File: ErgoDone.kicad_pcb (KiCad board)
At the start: 2 copper layers, 173.3 x 158.9 mm, 149 parts, among them J1 USB, J2 3.5mm, J3 JMP, J4 JMP, SW0:10 SW0:3, SW0:11 SW0:2, SW0:12 SW0:1, SW0:7 SW0:6, SW0:8 SW0:5, SW0:9 SW0:4, SW1:10 SW1:3, SW1:11 SW1:2, SW1:12 SW1:1, SW1:13 SW1:0, SW1:9 SW1:4, SW2:10 SW2:3, SW2:11 SW2:2, SW2:12 SW2:1, SW2:13 SW2:0, SW2:7 SW2:6, SW2:8 SW2:5, SW2:9 SW2:4, SW3:10 SW3:3, SW3:11 SW3:2, SW3:12 SW3:1, SW3:13 SW3:0, SW3:7 SW3:6, SW3:8 SW3:5, SW3:9 SW3:4, SW4:10 SW4:3, SW4:11 SW4:2, SW4:12 SW4:1, SW4:13 SW4:0, SW4:7 SW4:6, SW4:8 SW4:5, SW4:9 SW4:4, SW5:10 SW5:3, SW5:11 SW5:2, SW5:12 SW5:1, SW5:13 SW5:0, SW5:7 SW5:6, SW5:8 SW5:5, SW5:9 SW5:4, U1 ProMicro, U2 MCP23017

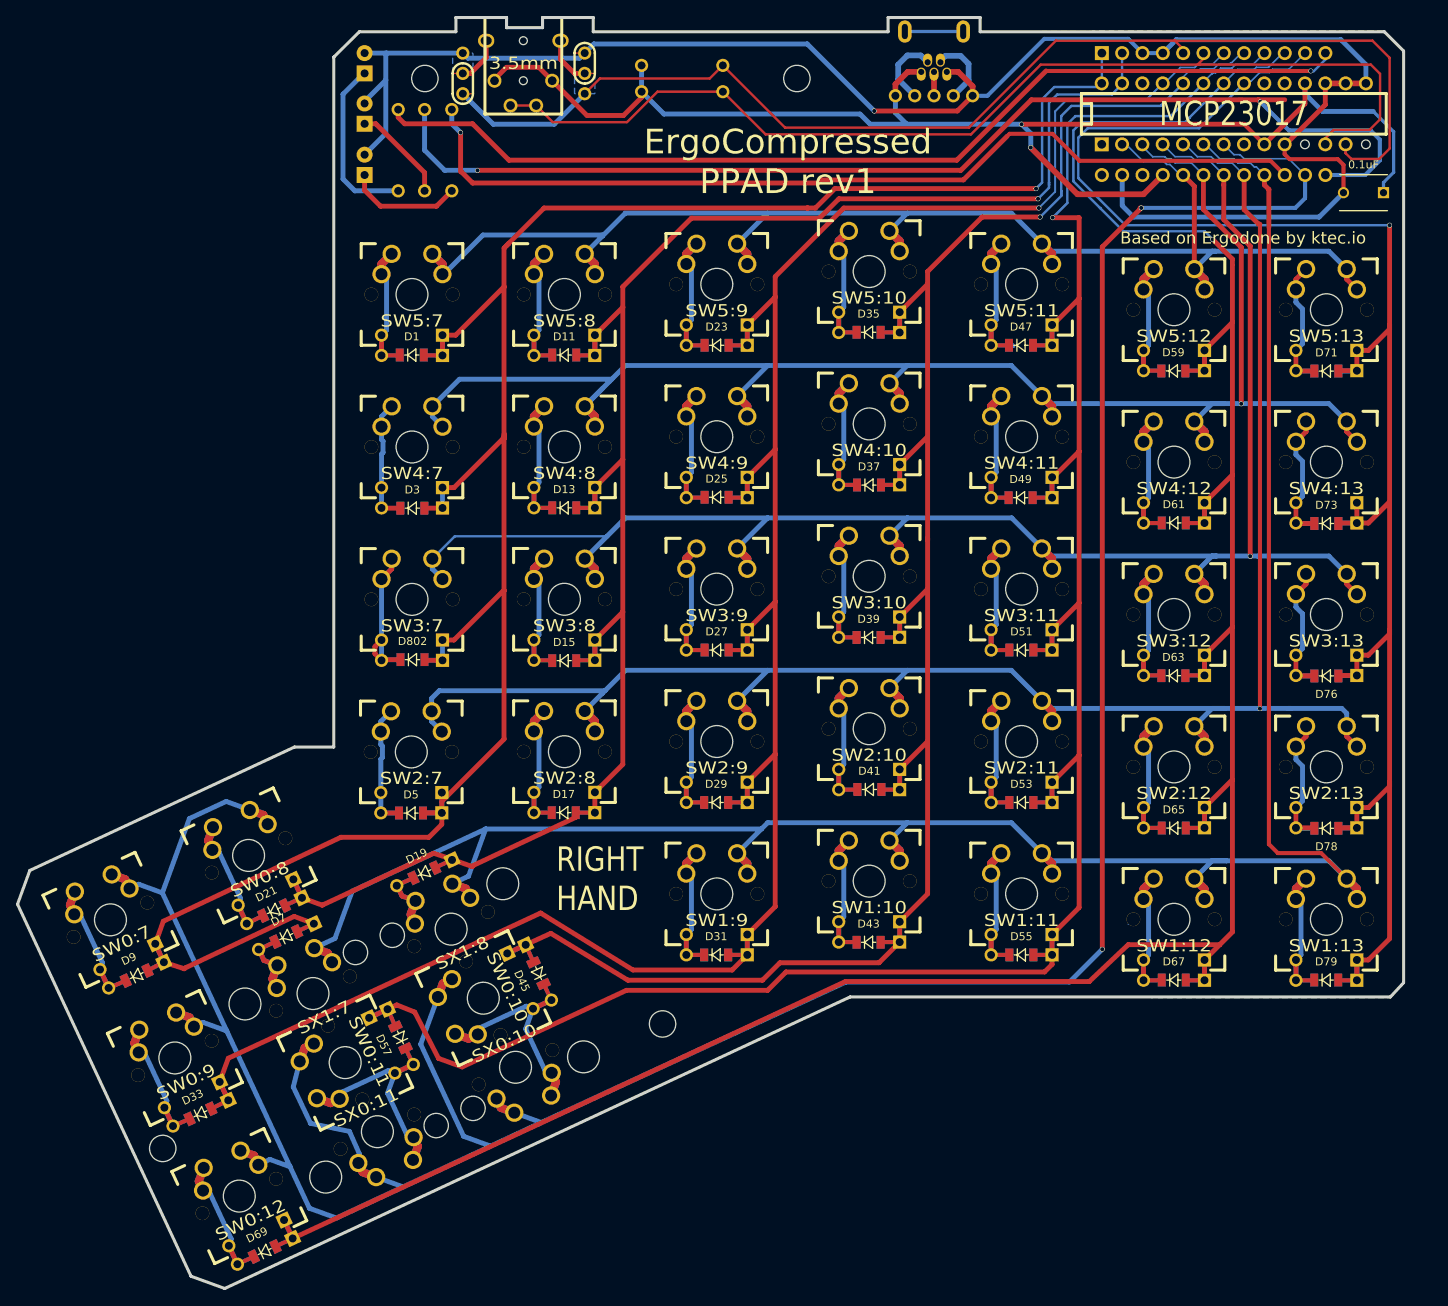
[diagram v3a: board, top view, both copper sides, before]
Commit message: Routing traces so the inner column of the thumb cluster could be safely removed.
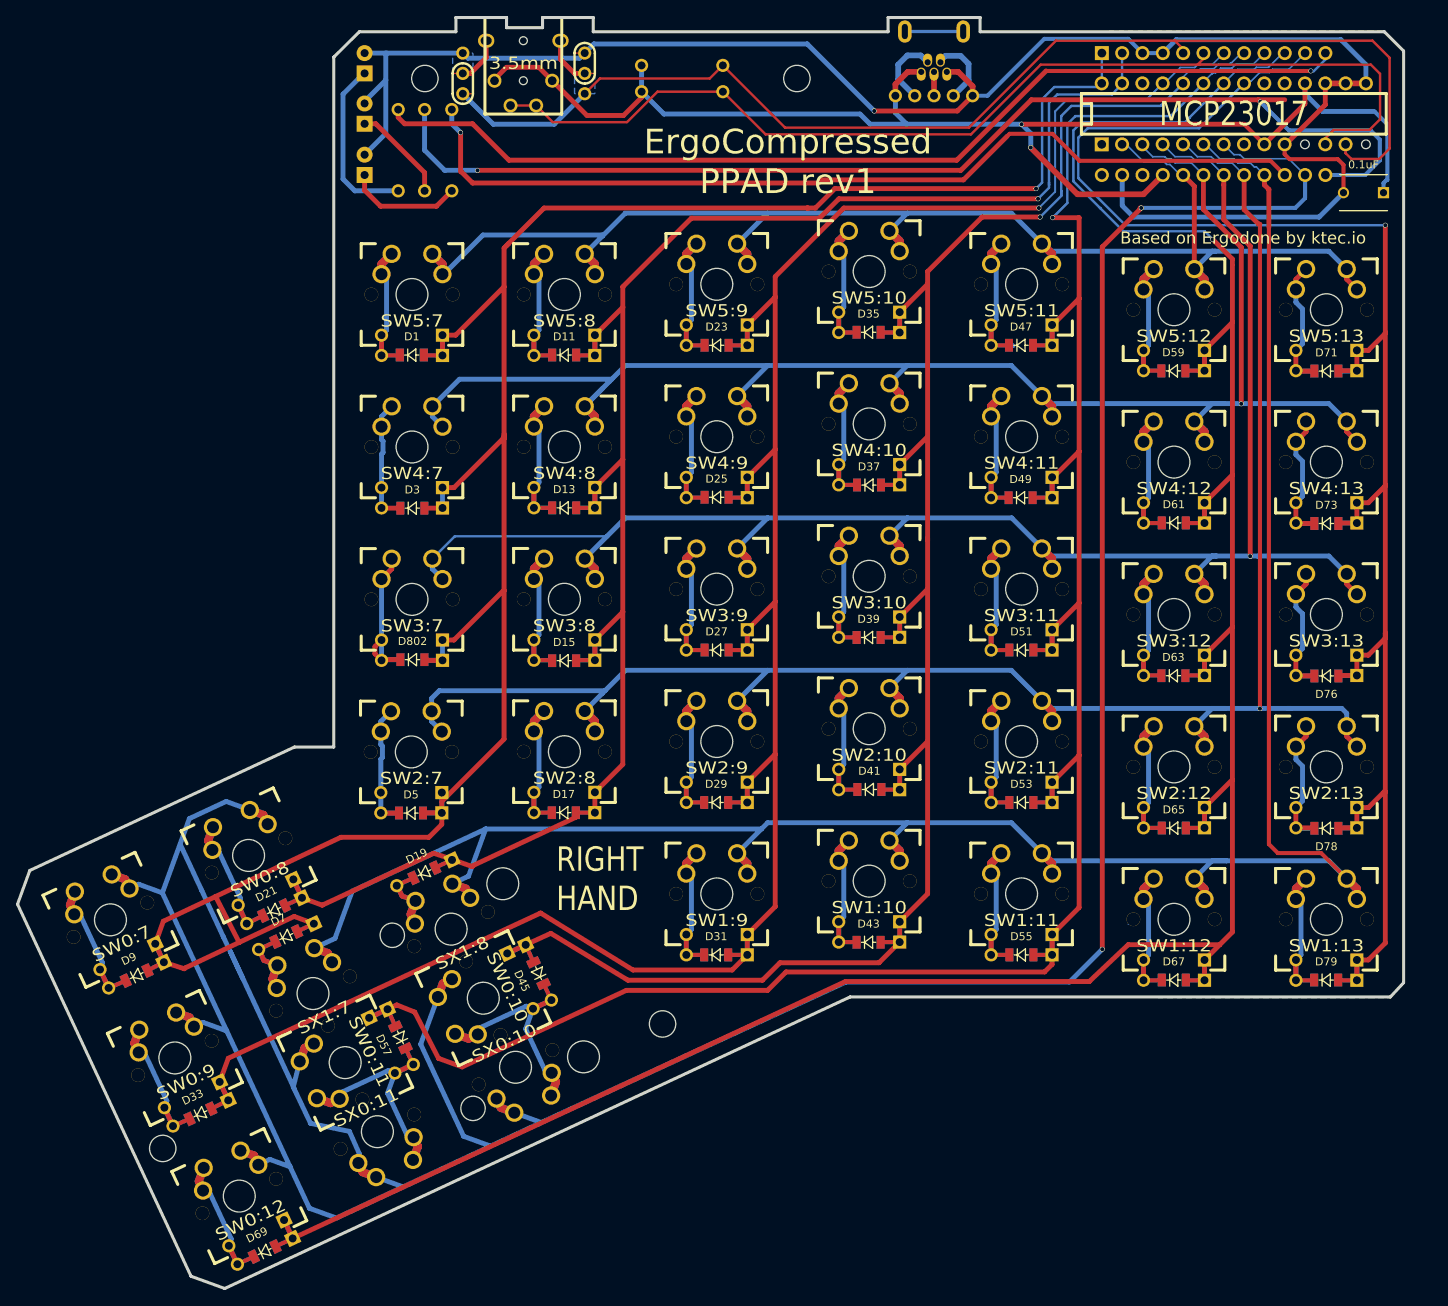
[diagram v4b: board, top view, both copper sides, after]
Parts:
- removed S1: STAB200, ErgoDone:STAB_PCB940
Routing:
- net /ROW0: track 410.6 -> 447.9 mm
- net /COL6: track 307.1 -> 313.6 mm
- net /COL0: track 235.0 -> 230.4 mm
- net VCC: track 173.7 -> 173.2 mm

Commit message: New cut, adjusting silkscreen, added Przemo-c
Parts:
- removed the REF** at (103.7, 156.3)
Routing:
- net /ROW0: track 447.9 -> 457.5 mm
- net /COL1: track 353.4 -> 361.8 mm
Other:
- outline, holes or cut-outs redrawn
- board text added: "ErgoCompressed"
- board text added: "PPAD rev1"
- board text added: "Przemo-c"
- board text removed: "ErgoCompressed PPAD rev1"
- board text removed: "LEFT HAND"
- board text removed: "RIGHT HAND"
- board text removed: "Ver 1.4"
